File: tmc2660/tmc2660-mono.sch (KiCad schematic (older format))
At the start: 16 parts, among them J1 0R, P3 Motor, U1 TMC2660

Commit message: Schematic lib update.
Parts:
- C1, C2, C3, C4, C5, C6: symbol C -> device:C
- C7, C8: symbol C_Small -> device:C_Small
- C9: symbol CP -> device:CP
- J1, R2, R3, R6, R7: symbol R -> device:R
- P3: symbol Conn_01x04 -> Connector:Conn_01x04
- U1: symbol TMC2660 -> tmc2660:TMC2660
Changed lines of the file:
@@
-EESchema Schematic File Version 3
-LIBS:power
-LIBS:device
-LIBS:linear
-LIBS:tmc2660
-LIBS:Connector
-LIBS:tmc2660-quad-cache
+EESchema Schematic File Version 4
+LIBS:tmc2660-mono-cache
 EELAYER 26 0
 EELAYER END
@@
 $EndDescr
 $Comp
-L C C4
+L device:C C4
 U 1 1 55767937
 P 4800 2700
@@
 $EndComp
 $Comp
-L C C5
+L device:C C5
 U 1 1 557679AB
 P 4800 3550
@@
 $EndComp
 $Comp
-L GND #PWR01
+L power:GND #PWR01
 U 1 1 55767A6C
 P 4800 3700
@@
 $EndComp
 $Comp
-L GND #PWR02
+L power:GND #PWR02
 U 1 1 55767A87
 P 4800 2850
@@
 $EndComp
 $Comp
-L C C2
+L device:C C2
 U 1 1 55767A9A
 P 3450 2250
@@
 	3950 2550 4800 2550
 $Comp
-L C C3
+L device:C C3
 U 1 1 55767EB4
 P 3750 2150
@@
 Connection ~ 3600 2000
 $Comp
-L GND #PWR03
+L power:GND #PWR03
 U 1 1 55767EEE
 P 3900 2300
@@
 Connection ~ 3350 4250
 $Comp
-L GND #PWR04
+L power:GND #PWR04
 U 1 1 5576833D
 P 3350 4250
@@
 Connection ~ 3950 3600
 $Comp
-L R R2
+L device:R R2
 U 1 1 557688AD
 P 4100 3150
@@
 $EndComp
 $Comp
-L R R3
+L device:R R3
 U 1 1 55768AD7
 P 4100 4000
@@
 $EndComp
 $Comp
-L GND #PWR05
+L power:GND #PWR05
 U 1 1 55768AE6
 P 4700 4150
@@
 	3950 2700 4150 2700
 $Comp
-L Conn_01x04 P3
+L Connector:Conn_01x04 P3
 U 1 1 5576913F
 P 5500 3300
@@
 1B2
 $Comp
-L C C1
+L device:C C1
 U 1 1 55769F99
 P 2750 3850
@@
 $EndComp
 $Comp
-L GND #PWR07
+L power:GND #PWR07
 U 1 1 55769FFF
 P 2600 3850
@@
 VMot
 $Comp
-L TMC2660 U1
+L tmc2660:TMC2660 U1
 U 1 1 5576B0C2
 P 3500 3300
@@
 1B2
 $Comp
-L GND #PWR08
+L power:GND #PWR08
 U 1 1 56711446
 P 2800 4300
@@
 $EndComp
 $Comp
-L C C6
+L device:C C6
 U 1 1 56711673
 P 2800 4150
@@
 Connection ~ 2800 4000
 $Comp
-L GND #PWR09
+L power:GND #PWR09
 U 1 1 5672E81A
 P 2550 2150
@@
 NoConn ~ 2900 3700
 $Comp
-L GND #PWR010
+L power:GND #PWR010
 U 1 1 5672F758
 P 2650 2600
@@
 VMot
 $Comp
-L GND #PWR011
+L power:GND #PWR011
 U 1 1 56739574
 P 3050 4250
@@
 $EndComp
 $Comp
-L R R7
+L device:R R7
 U 1 1 568D6888
 P 4500 4150
@@
 $EndComp
 $Comp
-L R R6
+L device:R R6
 U 1 1 568D6967
 P 4500 3300
@@
 Connection ~ 2800 2600
 $Comp
-L C_Small C7
+L device:C_Small C7
 U 1 1 568DEE7C
 P 4500 3150
@@
 	3950 2900 4150 2900
 $Comp
-L C_Small C8
+L device:C_Small C8
 U 1 1 568DF320
 P 4500 4000
@@
 DIR_1
 $Comp
-L VCC #PWR06
+L power:VCC #PWR06
 U 1 1 5A07DCFD
 P 2550 4000
@@
 Connection ~ 4350 3150
 $Comp
-L CP C9
+L device:CP C9
 U 1 1 5A081AAE
 P 4050 2150
@@
 GLOBAL_MISO
 $Comp
-L R J1
+L device:R J1
 U 1 1 5A0A53B6
 P 2250 2850

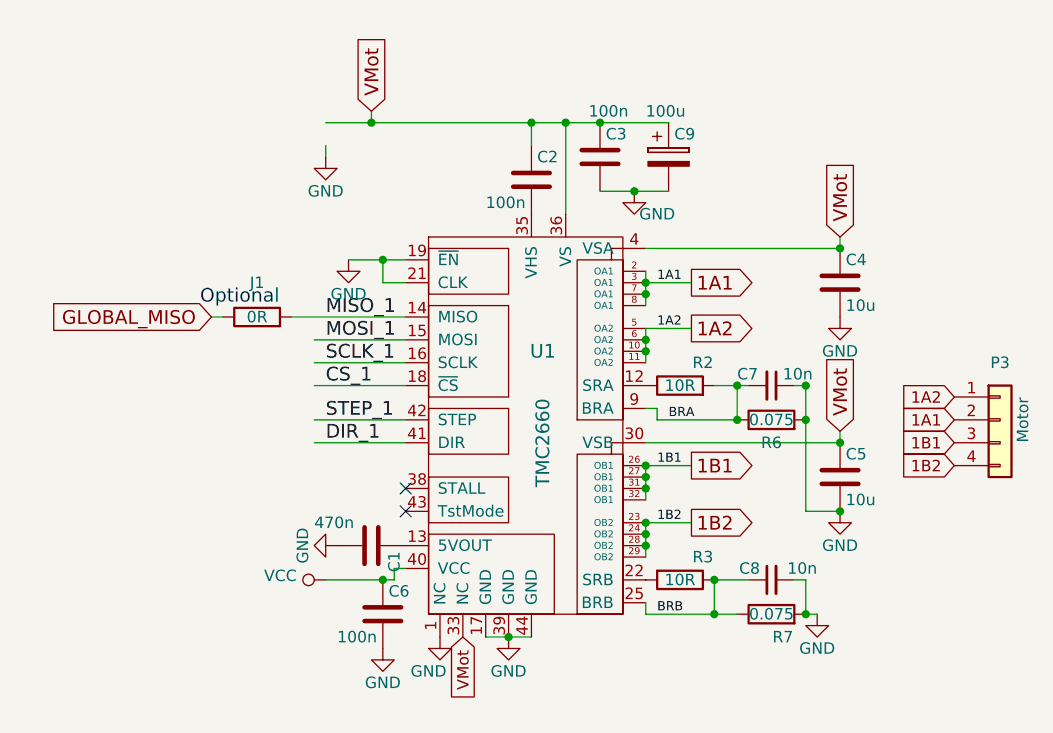
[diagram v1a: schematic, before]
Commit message: Add ~ENABLE to the bus.
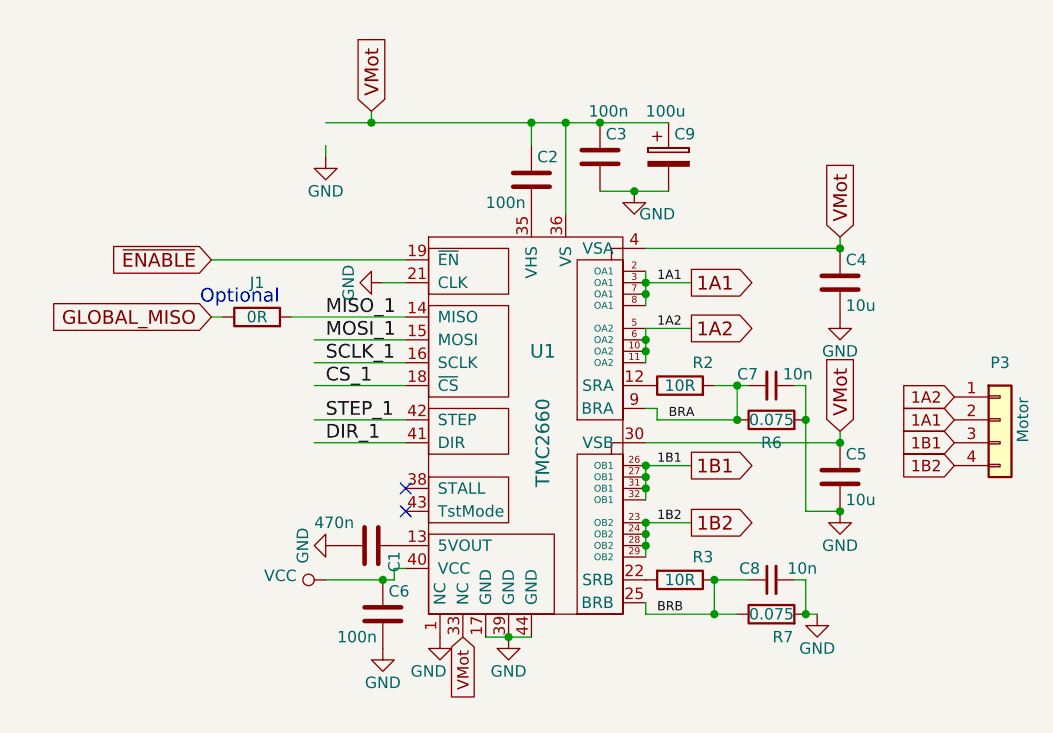
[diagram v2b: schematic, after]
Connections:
- net labels added: ~ENABLE
- wire segments 49 -> 48
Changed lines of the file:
@@
 L power:GND #PWR010
 U 1 1 5672F758
-P 2650 2600
-F 0 "#PWR010" H 2650 2350 50  0001 C CNN
-F 1 "GND" H 2650 2450 50  0000 C CNN
-F 2 "" H 2650 2600 60  0000 C CNN
-F 3 "" H 2650 2600 60  0000 C CNN
-	1    2650 2600
-	1    0    0    -1
-$EndComp
-Wire Wire Line
-	2650 2600 2900 2600
+P 2800 2700
+F 0 "#PWR010" H 2800 2450 50  0001 C CNN
+F 1 "GND" H 2800 2550 50  0000 C CNN
+F 2 "" H 2800 2700 60  0000 C CNN
+F 3 "" H 2800 2700 60  0000 C CNN
+	1    2800 2700
+	0    1    1    0
+$EndComp
+Wire Wire Line
+	2050 2600 2900 2600
 Wire Wire Line
 	2900 3950 2850 3950
 Wire Wire Line
-	2850 4000 2850 3950
-Wire Wire Line
-	2550 4000 2850 4000
+	2850 3950 2850 4000
+Wire Wire Line
+	2850 4000 2550 4000
 Text GLabel 3150 4250 3    50   Input ~ 0
 VMot
@@
 $EndComp
 Wire Wire Line
-	2800 2600 2800 2700
-Wire Wire Line
 	2800 2700 2900 2700
-Connection ~ 2800 2600
 $Comp
 L device:C_Small C7
@@
 	4650 4150 4700 4150
 Connection ~ 4650 4150
-Connection ~ 4650 3150
 Connection ~ 4350 3300
 Wire Wire Line
@@
 Text Notes 2000 2800 0    60   ~ 0
 Optional
+Text GLabel 2050 2600 0    60   Input ~ 0
+~ENABLE
 $EndSCHEMATC

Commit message: First transition into hierachical sheets.
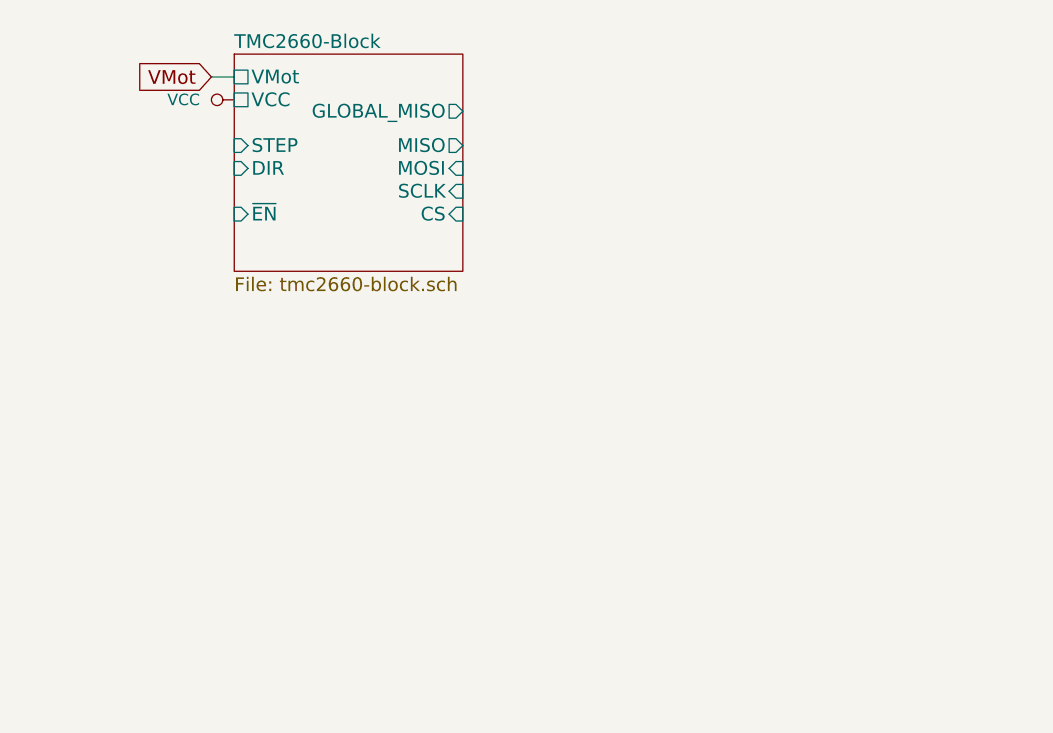
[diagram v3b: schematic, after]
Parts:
- removed C1: 470n, Capacitors_SMD:C_0603, symbol device:C
- removed C2, C3: 100n, Capacitors_SMD:C_0805, symbol device:C
- removed C4, C5: 10u, Capacitors_SMD:C_1206, symbol device:C
- removed C6: 100n, Capacitors_SMD:C_0603, symbol device:C
- removed C7, C8: 10n, Capacitors_SMD:C_0603, symbol device:C_Small
- removed C9: 100u, Capacitors_THT:CP_Radial_D10.0mm_P5.00mm, symbol device:CP
- removed J1: 0R, Resistors_SMD:R_0603, symbol device:R
- removed P3: Motor, Connectors_JST:JST_XH_B04B-XH-A_04x2.50mm_Straight, symbol Connector:Conn_01x04
- removed R2, R3: 10R, Resistors_SMD:R_0603, symbol device:R
- removed R6, R7: 0.075, Resistors_SMD:R_2512, symbol device:R
- removed U1: TMC2660, Housings_QFP:LQFP-44_10x10mm_Pitch0.8mm, symbol tmc2660:TMC2660
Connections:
- net labels removed: 1A1, 1A2, 1B1, 1B2, BRA, BRB, CS_1, DIR_1, GLOBAL_MISO, GND, MISO_1, MOSI_1, SCLK_1, STEP_1, ~ENABLE
- wire segments 48 -> 1
- no-connect marks 2 -> 0
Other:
- note removed: "Optional"
